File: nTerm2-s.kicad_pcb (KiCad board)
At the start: 2 copper layers, 147.3 x 55.9 mm, 107 parts, among them J1 VGA, J2 Keyboard, J3 Mouse, J4 Speaker, J5 DE9_Plug_MountingHoles, J6 USB_C_Receptacle_USB2.0_16P, K1 IM41 3V, K2 IM41 3V, K3 IM41 3V, Q1 BC817, Q2 BC817, Q3 BC817, Q4 BC817, Q5 BC817, SW1 IO0, SW2 RESET, SW3 DEFAULTS, U1 ESP32-WROOM-32, U2 LM386, U3 MAX3232E, U4 CP2102N-Axx-xQFN28, U5 NCP1117-3.3_SOT223

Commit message: v0.04
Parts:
- C23: value 100u -> 100u/25V
- U4: footprint Package_DFN_QFN:QFN-28-1EP_5x5mm_P0.5mm_EP3.35x3.35mm -> Package_DFN_QFN:QFN-28-1EP_5x5mm_P0.5mm_EP3.35x3.35mm_handsolder
- moved R21 8.46 mm to (167.1, 91.5)
- moved R26 5.31 mm to (105.5, 88.2), turned to 0 degrees
- moved R20 5.16 mm to (167.1, 93.7), turned to 0 degrees
- moved C3 4.62 mm to (168.0, 99.2), turned to -90 degrees
- moved R19 3.07 mm to (165.8, 99.2), turned to -90 degrees
- moved C17 3.01 mm to (105.0, 85.8)
- moved R29 2.93 mm to (105.5, 90.3), turned to 0 degrees
- moved C7 2.76 mm to (167.1, 95.9), turned to 0 degrees
- moved R31 1.56 mm to (92.8, 108.6)
- moved R40 0.93 mm to (92.8, 106.3)
- moved R39 0.30 mm to (92.8, 104.0)
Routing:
- net GND: track 182.4 -> 170.2 mm, vias 21 -> 23
- net AUDIO_PWM: track 66.9 -> 77.1 mm
- net EN: track 47.4 -> 56.0 mm
- net Net-(U2--): track 5.64 -> 9.05 mm
- net +3V3: track 250.0 -> 253.2 mm
- net REVERSE_RX_TX: track 102.7 -> 100.3 mm
- net REVERSE_RTS_CTS_DTR_DSR: track 68.4 -> 66.0 mm
- net Net-(U1-SENSOR_VN): track 45.5 -> 47.8 mm
- net Net-(Q1-E): track 36.8 -> 39.0 mm
- net VGA_VSYNC: track 34.4 -> 32.3 mm
- net Net-(J1-Pad2): track 57.3 -> 55.2 mm
- net Net-(J1-Pad1): track 57.3 -> 55.3 mm
- net Net-(J1-Pad3): track 57.3 -> 55.3 mm
- net Net-(J1-Pad13): track 55.6 -> 54.5 mm
- net RXD_0: track 59.1 -> 58.0 mm, vias 4 -> 2
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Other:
- board text removed: "Giants who'se shoulders I stand upon: Fabrizio Di Vittorio, Just4Fun, OMRON, Espressif, Silicon Labs, DEC, TI, KiCad, JLCPCB, Hackaday."

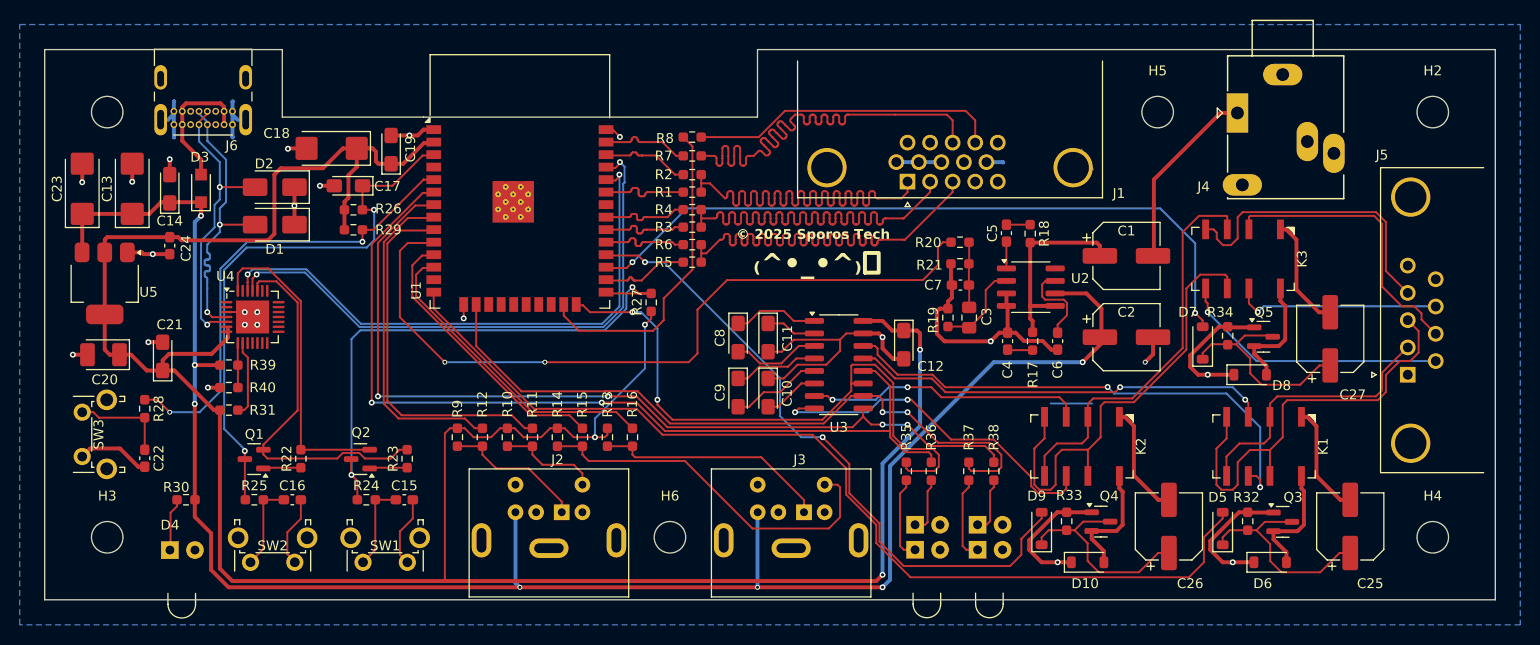
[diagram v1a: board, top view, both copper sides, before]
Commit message: nTerm2-S v0.05 - New PCBs ordered.
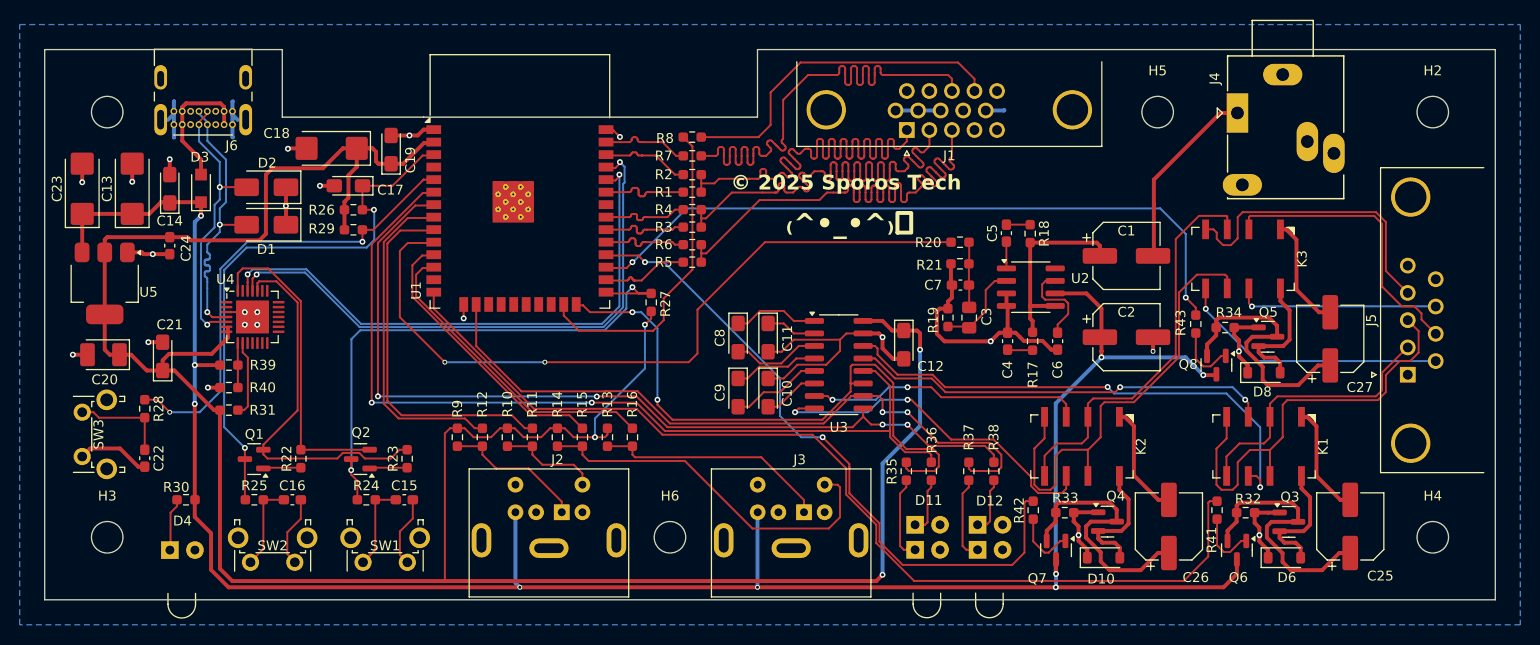
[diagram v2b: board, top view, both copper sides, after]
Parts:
- removed D5, D7, D9: BAT43W-V, Diode_SMD:D_SOD-123
- added Q6: BC817, Package_TO_SOT_SMD:SOT-23, F.Cu at (195.2, 122.8)
- added Q7: BC817, Package_TO_SOT_SMD:SOT-23, F.Cu at (176.8, 122.8)
- added Q8: BC817, Package_TO_SOT_SMD:SOT-23, F.Cu at (193.1, 104.0)
- added R41: 1K, Resistor_SMD:R_0603_1608Metric_Pad0.98x0.95mm_HandSolder, F.Cu at (193.2, 118.7)
- added R42: 1K, Resistor_SMD:R_0603_1608Metric_Pad0.98x0.95mm_HandSolder, F.Cu at (174.5, 118.7)
- added R43: 1K, Resistor_SMD:R_0603_1608Metric_Pad0.98x0.95mm_HandSolder, F.Cu at (191.0, 99.8)
- D11, D12: footprint LED_THT:DIALIGHT_LED_3MM_DOUBLE -> Sporos_Tech_Footprints:DIALIGHT_LED_3MM_DOUBLE
- D4: footprint LED_THT:DIALIGHT_LED_3MM_SINGLE -> Sporos_Tech_Footprints:DIALIGHT_LED_3MM_SINGLE
- J1: footprint Connector_Dsub:DSUB-15-HD_Female_Horizontal_P2.29x1.98mm_EdgePinOffset8.35mm_Housed_MountingHolesOffset10.89mm -> Sporos_Tech_Footprints:DSUB-15-HD_Female_Horizontal_P2.29x1.98mm_EdgePinOffset3.03mm_Housed_MountingHolesOffset4.94mm
- J4: footprint Connector_Audio:Jack_3.5mm_Ledino_KB3SPRS_Horizontal -> Sporos_Tech_Footprints:Jack_3.5mm_Ledino_KB3SPRS_Horizontal-alt
- J5: footprint Connector_Dsub:DSUB-9_Male_Horizontal_P2.77x2.84mm_EdgePinOffset4.94mm_Housed_MountingHolesOffset7.48mm -> Sporos_Tech_Footprints:DSUB-9_Male_Horizontal_P2.77x2.84mm_EdgePinOffset4.94mm_Housed_MountingHolesOffset7.48mm
- J6: footprint Connector_USB:USB_C_Receptacle_Molex_213716-0001 -> Sporos_Tech_Footprints:USB_C_Receptacle_Molex_213716-0001
- K1, K2, K3: footprint Relay_SMD:Relay_DPDT_AXICOM_IMSeries_Gullwing -> Sporos_Tech_Footprints:Relay_DPDT_AXICOM_IMSeries_Gullwing
- R32, R33, R34: value 3K9 -> 2K2
- SW1, SW2, SW3: footprint Button_Switch_THT:SW_Tactile_SPST_Angled_PTS645Vx58-2LFS -> Sporos_Tech_Footprints:SW_Tactile_SPST_Angled_PTS645Vx58-2LFS-alt
- U4: footprint Package_DFN_QFN:QFN-28-1EP_5x5mm_P0.5mm_EP3.35x3.35mm_handsolder -> Sporos_Tech_Footprints:QFN-28-1EP_5x5mm_P0.5mm_EP3.35x3.35mm_handsolder
- moved J1 5.24 mm to (161.7, 80.1)
- moved D10 1.68 mm to (181.6, 123.6)
- moved D6 1.52 mm to (200.0, 123.6)
- moved D8 1.41 mm to (197.9, 104.8)
- moved R32 0.90 mm to (196.1, 119.0), turned to 0 degrees
- moved R33 0.89 mm to (177.7, 119.0), turned to 0 degrees
- moved R34 0.87 mm to (194.0, 100.2), turned to 0 degrees
- moved D2 0.86 mm to (96.6, 86.0)
- moved D1 0.86 mm to (96.6, 89.8)
- moved Q4 0.67 mm to (182.0, 119.9)
- moved Q3 0.62 mm to (200.5, 119.9)
- moved Q5 0.44 mm to (198.3, 101.1)
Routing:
- net +5V: track 190.1 -> 229.5 mm, vias 7 -> 9
- net GND: track 170.2 -> 145.2 mm
- net Net-(Q7-B): track 0.00 -> 6.50 mm
- net Net-(Q8-B): track 0.00 -> 6.42 mm
- net Net-(Q6-B): track 0.00 -> 6.36 mm
- net Net-(Q5-C): track 21.5 -> 27.5 mm
- net Net-(Q3-C): track 21.6 -> 27.5 mm
- net Net-(Q4-C): track 21.6 -> 27.3 mm
- net Net-(J1-Pad3): track 55.3 -> 58.6 mm
- net Net-(J1-Pad2): track 55.2 -> 58.5 mm
- net Net-(J1-Pad1): track 55.3 -> 58.5 mm
- net Net-(J1-Pad13): track 54.5 -> 57.7 mm
- net Net-(J1-Pad14): track 31.6 -> 34.8 mm
- net REVERSE_RX_TX: track 100.3 -> 101.8 mm
- net RTS_CTS_OR_DTR_DSR: track 72.6 -> 71.1 mm
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
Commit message: V0.06 - Use USBLC6-2 for ESD protection, instead of those big TVS diodes. Those big TVS diodes were a bad choice, they have far too high a capacity for USB 2.0 use. Removed resistors from the bases of Q6, Q7 and Q8 as it only works reliably with very low resistance, and we might as well make them 0 ohm then. Added bypass capability for the audio amplifier, giving the user a choice to assemble it and drive a speaker, or save some money, don't assemble it and use line-out. Also a choice to solder a jackplug for external audio or use a connector for internal speaker.
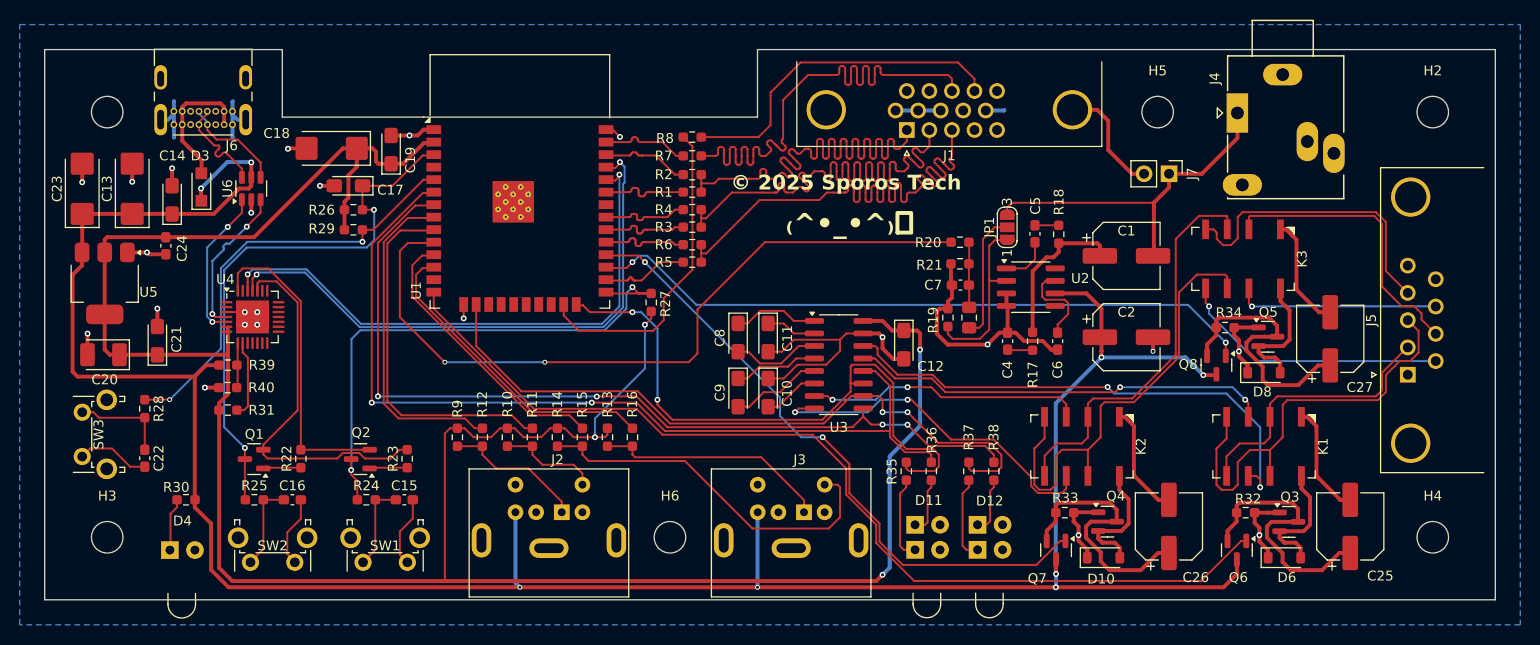
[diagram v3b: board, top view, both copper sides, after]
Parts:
- removed D1, D2: P4SMAJ5.0CA, Diode_SMD:D_SMA
- removed R41, R42, R43: 1K, Resistor_SMD:R_0603_1608Metric_Pad0.98x0.95mm_HandSolder
- added J7: Line-out/Speaker, Connector_PinHeader_2.54mm:PinHeader_1x02_P2.54mm_Vertical, F.Cu at (188.3, 84.6)
- added JP1: Bypass, Jumper:SolderJumper-3_P1.3mm_Open_RoundedPad1.0x1.5mm_NumberLabels, F.Cu at (171.9, 90.0)
- added U6: USBLC6-2SC6, Package_TO_SOT_SMD:SOT-23-6, F.Cu at (95.1, 86.1)
- J4: value Speaker -> Line-out/Speaker
- J5: value DE9_Plug_MountingHoles -> RS-232 V.24
- moved C5 2.90 mm to (174.7, 90.7)
- moved R18 2.90 mm to (177.1, 90.7)
- moved C21 1.68 mm to (85.5, 101.5)
- moved C14 1.15 mm to (87.0, 87.2)
- moved C24 0.40 mm to (86.4, 91.9)
- moved D3 0.14 mm to (90.0, 85.9)
- moved R40 0.13 mm to (92.7, 106.3)
- moved R31 0.10 mm to (92.7, 108.6)
- moved R39 0.10 mm to (92.7, 104.0)
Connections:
- C3 pad 2: Net-(U2--) -> Net-(JP1-C)
- J6 pad A6: Net-(D1-A2) -> Net-(J6-D+-PadA6)
- J6 pad A7: Net-(D2-A2) -> Net-(J6-D--PadA7)
- J6 pad B6: Net-(D1-A2) -> Net-(J6-D+-PadA6)
- J6 pad B7: Net-(D2-A2) -> Net-(J6-D--PadA7)
- Q6 pad 1: Net-(Q6-B) -> REVERSE_RX_TX
- Q7 pad 1: Net-(Q7-B) -> REVERSE_RTS_CTS_DTR_DSR
- Q8 pad 1: Net-(Q8-B) -> RTS_CTS_OR_DTR_DSR
- R19 pad 2: Net-(U2--) -> Net-(JP1-A)
- U2 pad 2: Net-(U2--) -> Net-(JP1-A)
- U4 pad 4: Net-(D1-A2) -> Net-(U4-D+)
- U4 pad 5: Net-(D2-A2) -> Net-(U4-D-)
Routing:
- net Net-(D2-A2): track 29.0 -> 0.00 mm, vias 2 -> 0
- net Net-(D1-A2): track 28.9 -> 0.00 mm, vias 2 -> 0
- net +5V: track 229.5 -> 252.7 mm, vias 9 -> 8
- net Net-(JP1-A): track 0.00 -> 17.8 mm
- net Net-(J7-Pin_1): track 19.1 -> 35.8 mm
- net Net-(U4-D-): track 0.00 -> 15.7 mm, vias 0 -> 2
- net Net-(U4-D+): track 0.00 -> 15.7 mm, vias 0 -> 2
- net Net-(JP1-C): track 0.00 -> 13.1 mm
- net Net-(J6-D+-PadA6): track 0.00 -> 10.6 mm
- net Net-(J6-D--PadA7): track 0.00 -> 10.5 mm
- net GND: track 145.2 -> 155.6 mm
- net Net-(U2--): track 9.05 -> 0.00 mm
- net Net-(Q7-B): track 6.50 -> 0.00 mm
- net Net-(Q8-B): track 6.42 -> 0.00 mm
- net Net-(Q6-B): track 6.36 -> 0.00 mm
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
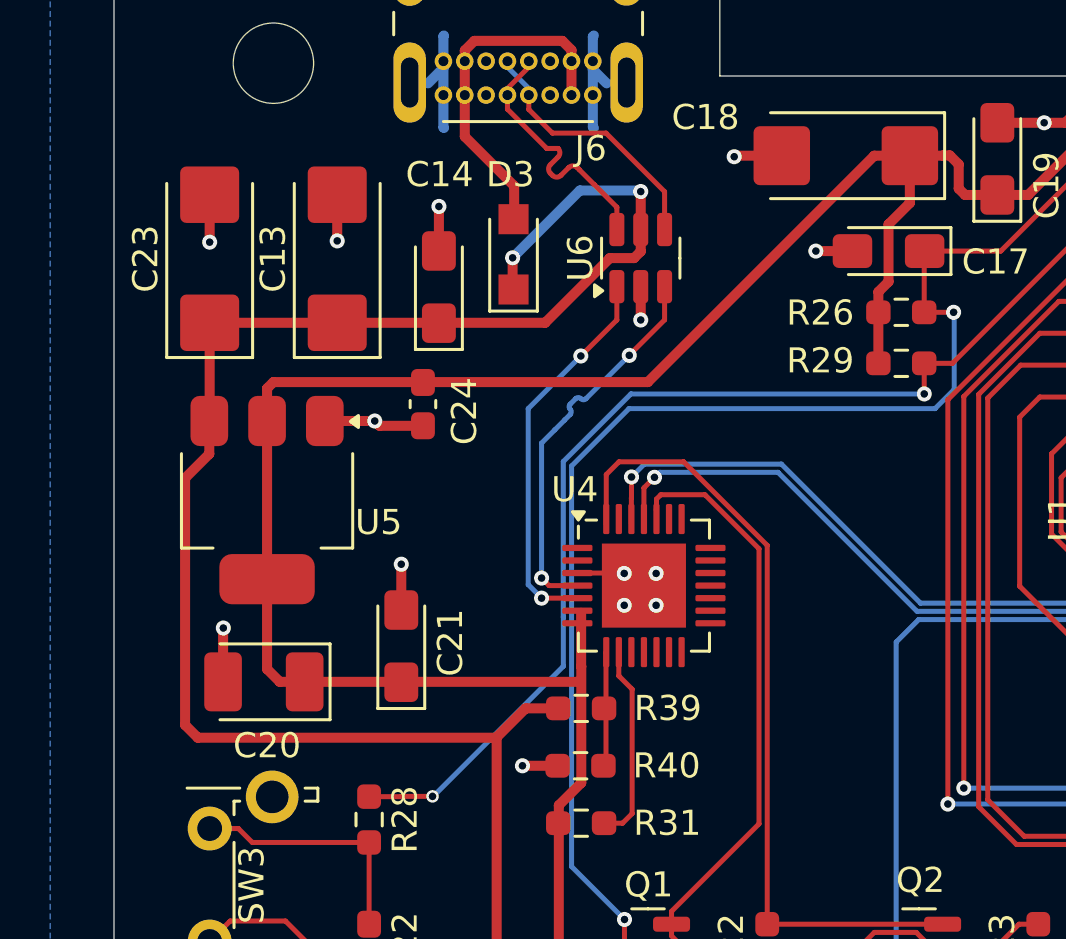
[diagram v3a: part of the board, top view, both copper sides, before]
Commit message: Update capacitor footprint to larger size.
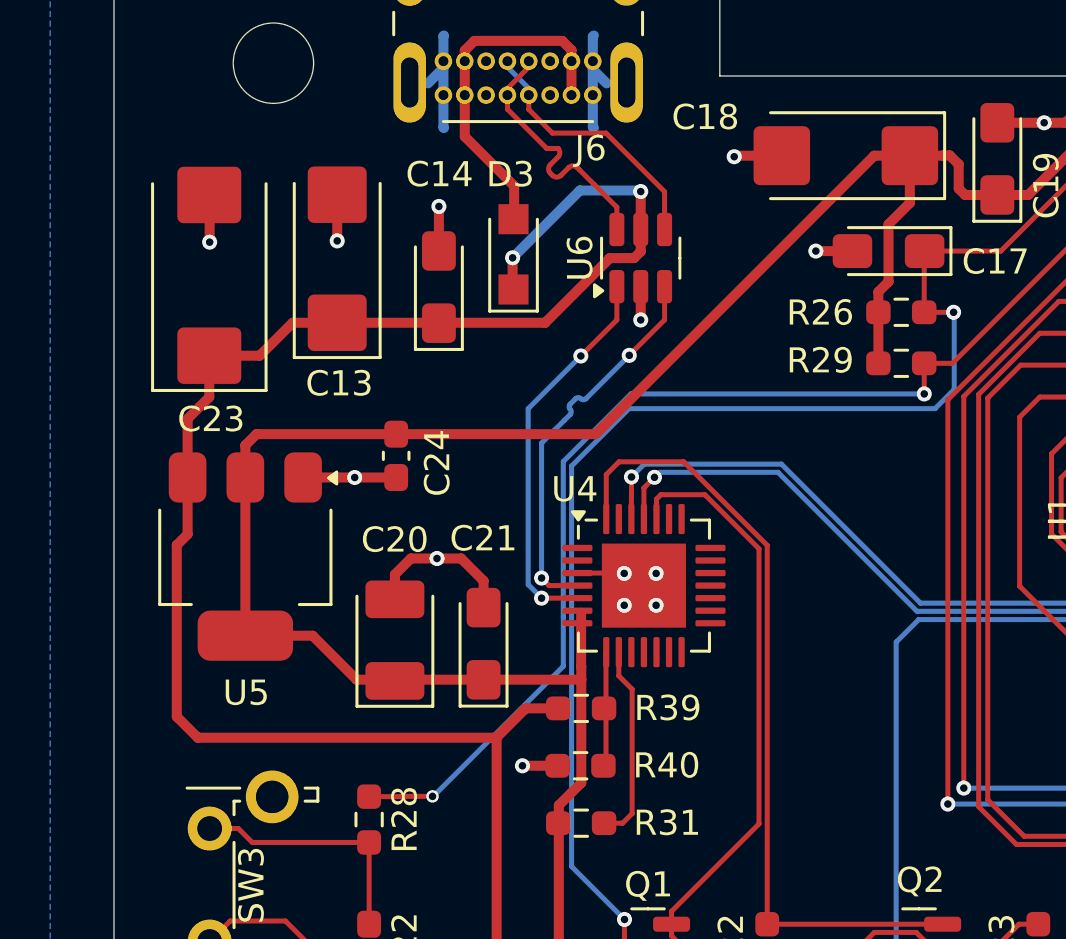
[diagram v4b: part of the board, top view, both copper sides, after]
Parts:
- C23: footprint Capacitor_Tantalum_SMD:CP_EIA-6032-28_Kemet-C_Pad2.25x2.35mm_HandSolder -> Capacitor_Tantalum_SMD:CP_EIA-7343-30_AVX-N_Pad2.25x2.55mm_HandSolder
- moved C20 5.48 mm to (85.3, 101.3), turned to 90 degrees
- moved C21 3.28 mm to (88.8, 101.4)
- moved U5 2.41 mm to (79.3, 98.0)
- moved C24 2.32 mm to (85.3, 94.0)
- moved C23 0.66 mm to (77.9, 86.8)
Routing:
- net GND: track 155.6 -> 157.3 mm, vias 23 -> 22
- net +5V: track 252.7 -> 251.9 mm
